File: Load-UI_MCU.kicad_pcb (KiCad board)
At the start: 4 copper layers, 85 x 90 mm, 117 parts, among them IC1 MSPM0G3519SPMR, IC2 TPS73533DRVT, IC3 TC4429CPA, IC4 TPS2121RUXR, J1 Conn_01x05_Socket, J10 Conn_01x02_Socket, J11 Conn_01x02_Socket, J12 Conn_01x02_Socket, J13 Conn_01x02_Socket, J14 Conn_01x02_Socket, J15 Conn_01x08_Pin, J16 Conn_01x02_Socket, J19 Conn_01x03_Socket, J2 Conn_01x06_Socket, J20 Conn_01x02_Socket, J21 Conn_01x02_Socket, J22 Conn_01x02_Socket, J23 Conn_01x02_Socket, J24 Conn_01x02_Socket, J3 Conn_01x02_Socket, J4 Conn_01x06_Socket, J5 Conn_01x02_Socket, J6 Conn_01x02_Socket, J7 Conn_01x02_Socket, J8 Conn_01x06_Socket, J9 Conn_01x03_Socket, Q2 2N2219, SW1 SW_Push, SW2 SW_Push, SW3 SW_Push_DPDT, U1 INA229AQDGSRQ1, U2 INA229AQDGSRQ1, U3 SN74HC14N, U4 SN74HC14N

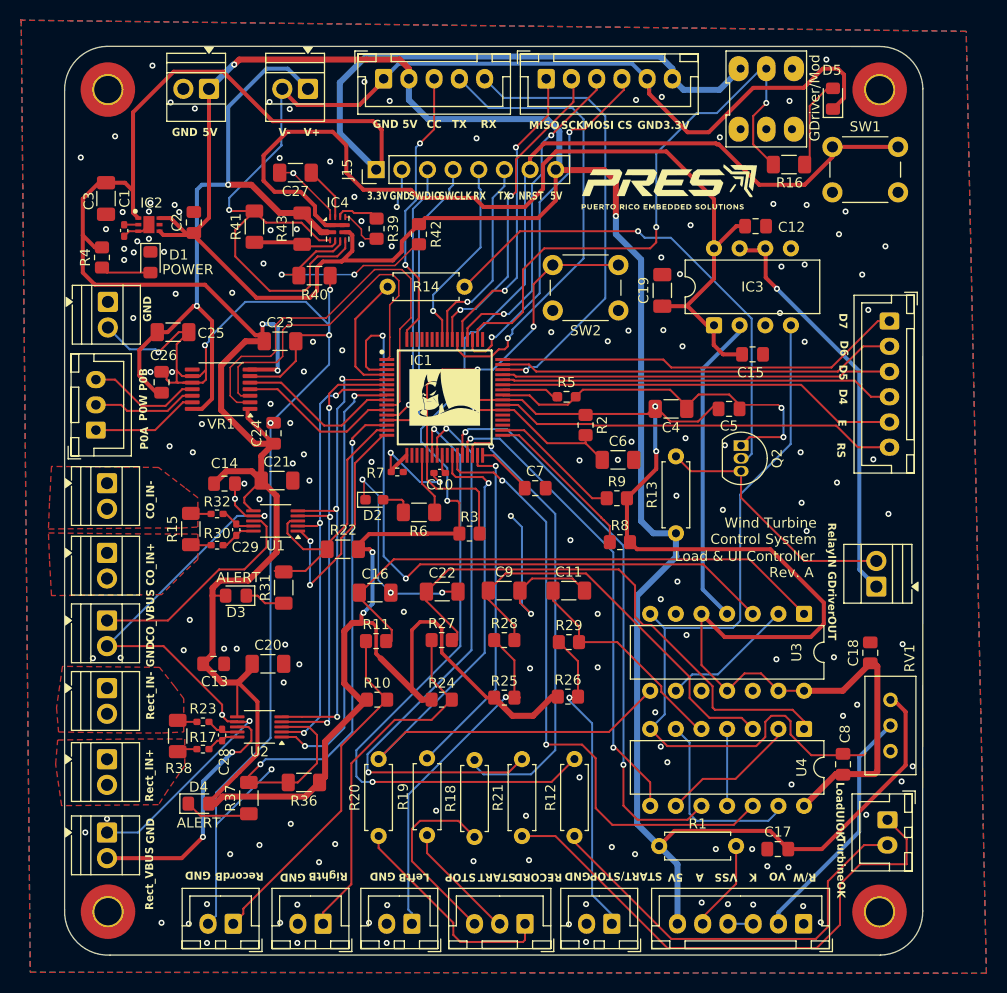
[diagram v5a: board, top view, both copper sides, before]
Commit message: Removed unnecessary hex inverter, fixed record button connection, change relay resistors to smd
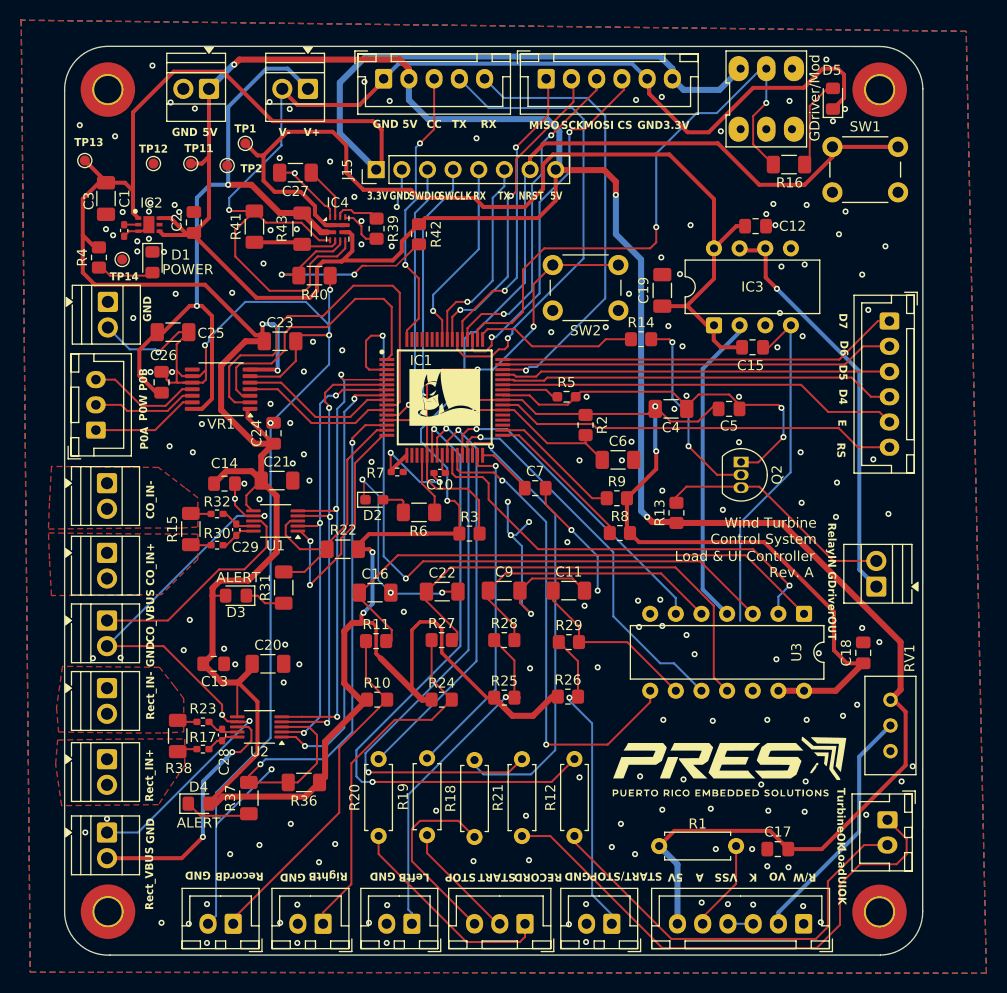
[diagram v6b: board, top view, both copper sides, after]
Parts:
- removed C8: 100n, Capacitor_SMD:C_0805_2012Metric_Pad1.18x1.45mm_HandSolder
- removed U4: SN74HC14N, Package_DIP:CERDIP-14_W7.62mm_SideBrazed
- added TP1: TestPoint, TestPoint:TestPoint_Pad_D1.0mm, F.Cu at (134.9, 59.6)
- added TP11: TestPoint, TestPoint:TestPoint_Pad_D1.0mm, F.Cu at (129.5, 61.6)
- added TP12: TestPoint, TestPoint:TestPoint_Pad_D1.0mm, F.Cu at (125.8, 61.6)
- added TP13: TestPoint, TestPoint:TestPoint_Pad_D1.0mm, F.Cu at (119.0, 61.3)
- added TP14: TestPoint, TestPoint:TestPoint_Pad_D1.0mm, F.Cu at (122.7, 71.1)
- added TP2: TestPoint, TestPoint:TestPoint_Pad_D1.0mm, F.Cu at (133.1, 61.8)
- R13, R14: footprint Resistor_THT:R_Axial_DIN0207_L6.3mm_D2.5mm_P7.62mm_Horizontal -> Resistor_SMD:R_0805_2012Metric_Pad1.20x1.40mm_HandSolder
- moved G*** 57.8 mm to (182.6, 121.7)
- moved R14 25.6 mm to (174.1, 79.0)
- moved R13 2.02 mm to (177.6, 96.2)
- moved Q2 1.63 mm to (184.0, 91.2)
- moved R8 0.90 mm to (172.0, 98.2)
- moved C18 0.70 mm to (196.1, 110.1)
- moved C15 0.70 mm to (185.1, 79.8)
- moved R4 0.30 mm to (120.4, 70.9)
- moved D1 0.20 mm to (125.7, 71.4)
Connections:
- net Net-(C16-Pad1) renamed RECORD_INPUT
- C11 pad 1: Net-(C11-Pad1) -> ST_INPUT
- C22 pad 1: Net-(C22-Pad1) -> RIGHT_INPUT
- C9 pad 1: Net-(C9-Pad1) -> LEFT_INPUT
- IC1 pad 25: unconnected-(IC1-PA24_/_A0_3-Pad25) -> RECORD_LED
- IC1 pad 4: Switch_Relay -> unconnected-(IC1-PB16-Pad4)
- IC1 pad 49: unconnected-(IC1-PA7_/_CLK_OUT-Pad49) -> Switch_Relay
- R20 pad 2: RECORD -> RECORD_LED
- R27 pad 2: Net-(C22-Pad1) -> RIGHT_INPUT
- R28 pad 2: Net-(C9-Pad1) -> LEFT_INPUT
- R29 pad 2: Net-(C11-Pad1) -> ST_INPUT
- U3 pad 10: unconnected-(U3-Pad10) -> RIGHT
- U3 pad 11: +3.3V -> RIGHT_INPUT
- U3 pad 2: /UI/NOT_RECORD -> RECORD
- U3 pad 5: +3.3V -> LEFT_INPUT
- U3 pad 6: unconnected-(U3-Pad6) -> LEFT
- U3 pad 8: RECORD -> START/STOP
- U3 pad 9: /UI/NOT_RECORD -> ST_INPUT
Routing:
- net Net-(C22-Pad1): track 54.4 -> 0.00 mm
- net RIGHT_INPUT: track 0.00 -> 46.1 mm
- net +3.3V: track 460.2 -> 419.5 mm
- net Net-(C9-Pad1): track 40.5 -> 0.00 mm
- net RECORD_LED: track 0.00 -> 40.3 mm, vias 0 -> 1
- net LEFT_INPUT: track 0.00 -> 29.4 mm
- net Net-(Q2-B): track 48.9 -> 19.6 mm, vias 1 -> 2
- net GND: track 492.0 -> 465.6 mm, vias 172 -> 196
- net LEFT: track 57.6 -> 31.9 mm, vias 2 -> 1
- net RECORD: track 67.3 -> 44.0 mm
- net Net-(C11-Pad1): track 22.2 -> 0.00 mm
- net /UI/NOT_START/STOP: track 18.9 -> 0.00 mm
- net ST_INPUT: track 0.00 -> 17.8 mm
- net START/STOP: track 61.8 -> 47.6 mm
- net /UI/NOT_RIGHT: track 13.7 -> 0.00 mm
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
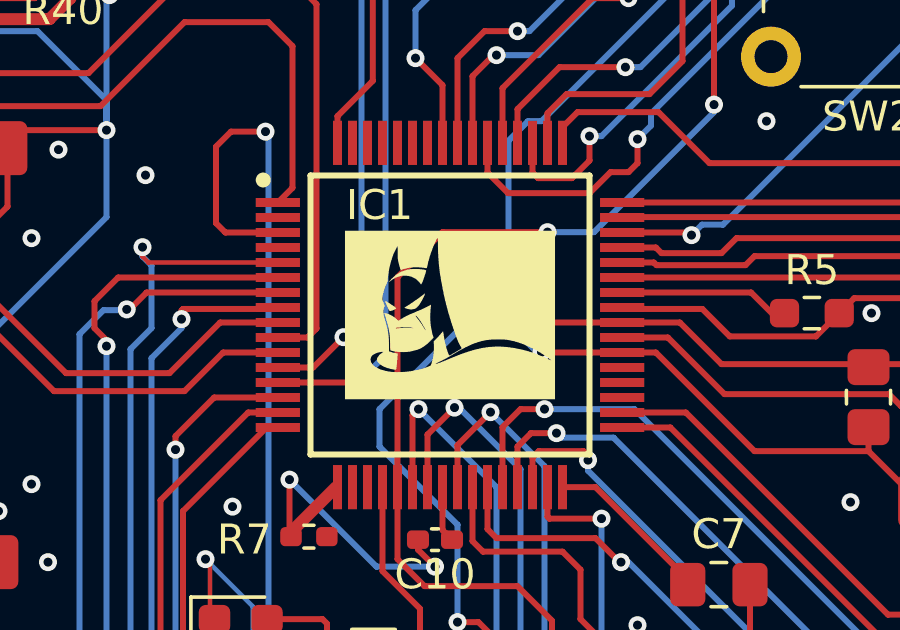
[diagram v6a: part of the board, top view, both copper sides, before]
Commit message: Added testpoints
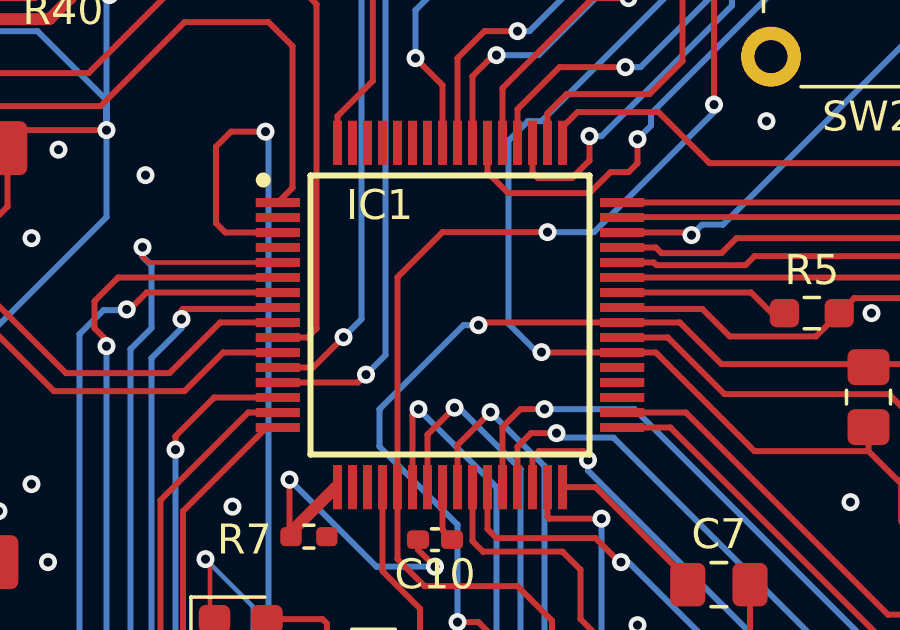
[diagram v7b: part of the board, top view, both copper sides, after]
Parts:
- removed the G*** at (154.7, 84.8)

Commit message: Last update after PR4, mostly done I need revisions from rest of members with special attention on grounding layout
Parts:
- removed C27: 10n, Capacitor_SMD:C_1206_3216Metric_Pad1.33x1.80mm_HandSolder
- removed D5: LED, LED_SMD:LED_0805_2012Metric_Pad1.15x1.40mm_HandSolder
- removed IC4: TPS2121RUXR, Package_DFN_QFN:Texas_VQFN-HR-12_2x2.5mm_P0.5mm
- removed R16: 1k, Resistor_SMD:R_1206_3216Metric_Pad1.30x1.75mm_HandSolder
- removed R39: 51k, Resistor_SMD:R_0805_2012Metric_Pad1.20x1.40mm_HandSolder
- removed R40, R41: 4.7k, Resistor_SMD:R_1206_3216Metric_Pad1.30x1.75mm_HandSolder
- removed R42: 24k, Resistor_SMD:R_0805_2012Metric_Pad1.20x1.40mm_HandSolder
- removed R43: 100k, Resistor_SMD:R_1206_3216Metric_Pad1.30x1.75mm_HandSolder
- removed SW3: SW_Push_DPDT, Latch_PB:SW_DPDT_XLX
- removed TP1, TP2: TestPoint, TestPoint:TestPoint_Pad_D1.0mm
- added D6: LED, LED_SMD:LED_0805_2012Metric_Pad1.15x1.40mm_HandSolder, F.Cu at (193.2, 55.2)
- added R33: 1k, Resistor_SMD:R_1206_3216Metric_Pad1.30x1.75mm_HandSolder, F.Cu at (188.9, 61.7)
- added SW4: SW_Push_DPDT, Latch_PB:SW_DPDT_XLX, F.Cu at (186.5, 55.1)
- R8, R9: value 47k -> 1k
- moved TP13 9.00 mm to (128.0, 61.0)
- moved TP12 8.82 mm to (134.6, 61.3)
- moved C1 8.82 mm to (129.9, 64.8)
- moved C2 8.82 mm to (138.6, 67.2)
- moved C3 8.82 mm to (131.7, 68.0)
- moved IC2 8.82 mm to (134.2, 67.4)
- moved R4 8.82 mm to (129.2, 70.6)
- moved D1 8.82 mm to (134.5, 71.1)
- moved TP14 8.82 mm to (131.5, 70.8)
- moved TP11 7.85 mm to (137.3, 60.7)
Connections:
- net Net-(IC3-INPUT) renamed NOT_Converter_Duty
- C12 pad 1: Highest_Power_Supply -> +5V
- C15 pad 1: Highest_Power_Supply -> +5V
- C19 pad 1: Highest_Power_Supply -> +5V
- IC1 pad 10: /Load/POT_SCK -> /Load/ConverterOUT_SCLK
- IC1 pad 11: /Load/POT_MOSI -> /Load/ConverterOUT_MOSI
- IC1 pad 60: unconnected-(IC1-PB8-Pad60) -> SCL
- IC1 pad 61: unconnected-(IC1-PB9-Pad61) -> SDA
- IC1 pad 9: /Load/POT_MISO -> /Load/ConverterOUT_MISO
- IC3 pad 1: Highest_Power_Supply -> +5V
- IC3 pad 8: Highest_Power_Supply -> +5V
- U1 pad 2: /Load/ConverterIN_MOSI -> /Load/ConverterOUT_MOSI
- U1 pad 4: /Load/ConverterIN_MISO -> /Load/ConverterOUT_MISO
- U1 pad 5: /Load/ConverterIN_SCLK -> /Load/ConverterOUT_SCLK
- VR1 pad 2: /Load/POT_SCK -> SCL
- VR1 pad 3: POT_CS -> GND
- VR1 pad 4: /Load/POT_MOSI -> SDA
- VR1 pad 5: /Load/POT_MISO -> GND
- VR1 pad 7: +3.3V -> unconnected-(VR1-NC-Pad7)
- VR1 pad 8: unconnected-(VR1-N/C-Pad8) -> +3.3V
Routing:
- net Highest_Power_Supply: track 97.0 -> 0.00 mm
- net /Load/POT_SCK: track 39.4 -> 0.00 mm
- net POT_CS: track 28.8 -> 0.00 mm
- net /Load/ConverterOUT_SCLK: track 0.00 -> 24.9 mm, vias 0 -> 2
- net SCL: track 0.00 -> 24.8 mm
- net SDA: track 0.00 -> 23.5 mm
- net Net-(IC4-OV1): track 23.2 -> 0.00 mm, vias 2 -> 0
- net +5V: track 242.9 -> 265.8 mm
- net /Load/ConverterOUT_MISO: track 0.00 -> 17.0 mm
- net /Load/ConverterOUT_MOSI: track 0.00 -> 16.4 mm
- net /Load/POT_MISO: track 15.8 -> 0.00 mm
- net /Load/POT_MOSI: track 15.6 -> 0.00 mm
- net +3.3V: track 419.5 -> 404.0 mm
- net GateDriver_OUT: track 40.4 -> 50.0 mm
- net Net-(D6-A): track 0.00 -> 9.03 mm
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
